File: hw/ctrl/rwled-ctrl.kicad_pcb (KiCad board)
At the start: 2 copper layers, 70.9 x 38.1 mm, 49 parts, among them J21 batt-chg, J31 USB_B_Micro, J61 led-a, J62 led-b, J63 led-c, J64 led-d, J65 batt-ab, J66 batt-cd, Q31 UMH3N, Q61 IRF4905STRLPBF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

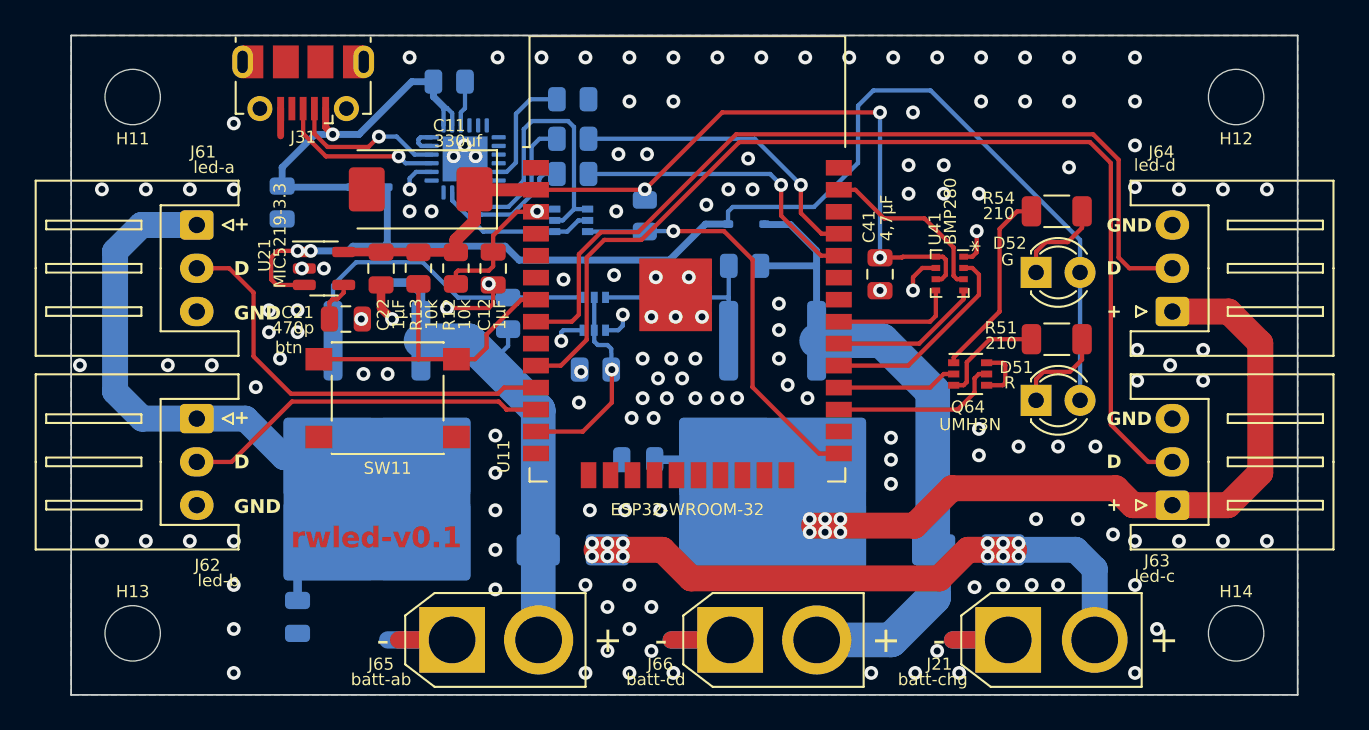
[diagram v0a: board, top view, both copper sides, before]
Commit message: hw - доработки платы под oled-дисплей
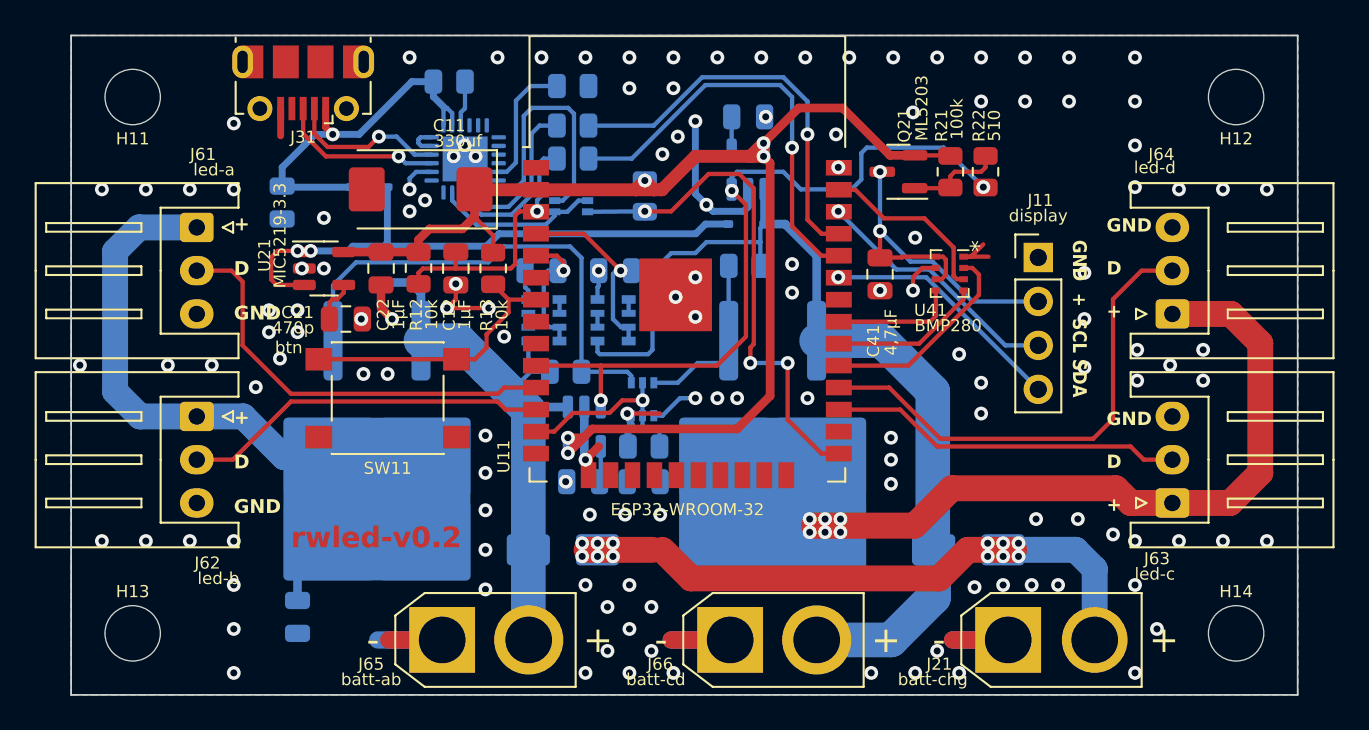
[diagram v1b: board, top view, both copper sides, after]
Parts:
- removed D51: R, LED_THT:LED_D3.0mm
- removed D52: G, LED_THT:LED_D3.0mm
- removed Q64: UMH3N, Package_TO_SOT_SMD:SOT-363_SC-70-6
- removed R51, R54: 210, Resistor_SMD:R_1206_3216Metric
- added C24: 470p, Capacitor_SMD:C_0805_2012Metric, B.Cu at (133.2, 67.7)
- added C25: 1μF, Capacitor_SMD:C_0805_2012Metric, B.Cu at (130.8, 55.5)
- added C26: 470p, Capacitor_SMD:C_0805_2012Metric, B.Cu at (142.7, 46.6)
- added C27: 1μF, Capacitor_SMD:C_0805_2012Metric, B.Cu at (135.1, 55.5)
- added J11: display, Connector_PinHeader_2.54mm:PinHeader_1x04_P2.54mm_Vertical, F.Cu at (159.5, 54.7)
- added Q21: ML5203, Package_TO_SOT_SMD:SOT-23, F.Cu at (151.4, 49.8)
- added R21: 100k, Resistor_SMD:R_0805_2012Metric, F.Cu at (154.4, 49.8)
- added R22: 510, Resistor_SMD:R_0805_2012Metric, F.Cu at (156.5, 49.8)
- added RN21: 100k, Resistor_SMD:R_Array_Convex_4x0603, B.Cu at (130.9, 58.4)
- added RN22: 100k, Resistor_SMD:R_Array_Convex_4x0603, B.Cu at (134.9, 58.4)
- added U22: MIC5219, Package_TO_SOT_SMD:SOT-23-5, B.Cu at (133.3, 64.5)
- added U23: MIC5219-3.3, Package_TO_SOT_SMD:SOT-23-5, B.Cu at (142.7, 49.7)
- moved Q63 5.67 mm to (136.6, 62.9)
- moved R64 5.25 mm to (136.7, 65.7)
- moved R61 4.74 mm to (132.2, 61.3), turned to 180 degrees
- moved R13 4.32 mm to (128.0, 55.4)
- moved C12 2.16 mm to (125.9, 55.4)
- moved R12 2.16 mm to (123.7, 55.4)
- moved C62 1.31 mm to (136.7, 67.7)
- moved Q31 1.14 mm to (132.5, 51.5)
- moved R11 1.14 mm to (136.8, 51.2)
- moved R32 0.89 mm to (132.6, 49.0)
- moved R33 0.76 mm to (132.6, 47.1)
- moved R34 0.76 mm to (132.6, 44.8)
- moved D24 0.57 mm to (132.0, 71.6)
- moved J65 0.57 mm to (125.1, 76.8)
- moved J61 0.14 mm to (110.9, 53.0)
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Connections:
- C41 pad 1: +3.3V -> +3.3VA
- U11 pad 10: /ldata-c -> hwen
- U11 pad 27: /led-r -> /ldata-c
- U11 pad 28: /led-g -> /ldata-d
- U11 pad 4: unconnected-(U11-SENSOR_VP-Pad4) -> Net-(RN22-R1.2)
- U11 pad 5: unconnected-(U11-SENSOR_VN-Pad5) -> Net-(RN21-R1.2)
- U11 pad 8: /ldata-d -> unconnected-(U11-IO32-Pad8)
- U41 pad 6: +3.3V -> +3.3VA
- U41 pad 8: +3.3V -> +3.3VA
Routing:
- net hwen: track 0.00 -> 42.4 mm, vias 0 -> 3
- net /ldata-c: track 61.4 -> 20.5 mm
- net +5V: track 73.3 -> 33.9 mm
- net +3.3V: track 50.5 -> 74.6 mm, vias 3 -> 5
- net +3.3VA: track 0.00 -> 21.5 mm, vias 0 -> 2
- net /ldata-d: track 49.8 -> 28.6 mm
- net GND: track 41.0 -> 59.0 mm, vias 156 -> 139
- net +BATT-CD: track 39.7 -> 56.3 mm
- net i2c-scl: track 0.00 -> 14.8 mm, vias 0 -> 1
- net i2c-sda: track 0.00 -> 14.2 mm, vias 0 -> 1
- net Net-(RN22-R1.2): track 0.00 -> 11.4 mm, vias 0 -> 1
- net Net-(Q64A-E1): track 11.1 -> 0.00 mm
- net /led-r: track 9.87 -> 0.00 mm
- net Net-(Q61-G): track 19.0 -> 28.7 mm
- net Net-(RN21-R1.2): track 0.00 -> 8.32 mm, vias 0 -> 1
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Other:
- board text added: "GND + SCL SDA"
- board text added: "rwled-v0.2"
- board text removed: "rwled-v0.1"

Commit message: hw - архив доработанных и отправленных в заказ плат
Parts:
- removed C24, C26: 470p, Capacitor_SMD:C_0805_2012Metric
- removed U22: MIC5219, Package_TO_SOT_SMD:SOT-23-5
- removed U23: MIC5219-3.3, Package_TO_SOT_SMD:SOT-23-5
- added R23: 10k, Resistor_SMD:R_0805_2012Metric, F.Cu at (115.1, 55.4)
- U21: value MIC5219-3.3 -> MIC5219
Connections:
- Q63 pad 1: Net-(Q61-G) -> GND
- Q63 pad 6: GND -> Net-(Q61-G)
- U21 pad 3: +5V -> Net-(U21-EN)
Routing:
- net +3.3V: track 74.6 -> 45.1 mm, vias 5 -> 1
- net GND: track 59.0 -> 48.0 mm, vias 139 -> 144
- net hwen: track 42.4 -> 37.7 mm, vias 3 -> 2
- net +5V: track 33.9 -> 30.6 mm
- net +BATT-AB: track 33.1 -> 30.8 mm
- net Net-(U22-BP): track 2.06 -> 0.00 mm
- net Net-(U21-EN): track 0.00 -> 2.06 mm
- net +BATT-CD: track 56.3 -> 54.3 mm
- net Net-(U23-BP): track 1.92 -> 0.00 mm
- net Net-(Q61-G): track 28.7 -> 30.4 mm
- net /s-boot: track 30.5 -> 29.5 mm, vias 3 -> 1
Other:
- board text added: "rwled-v0.2a"
- board text removed: "rwled-v0.2"
